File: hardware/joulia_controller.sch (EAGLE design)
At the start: 46 parts, among them IC1 LM2902D, IC2 LM2902D, U1 MMBT2222ALT1G, U2 MMBT2222ALT1G

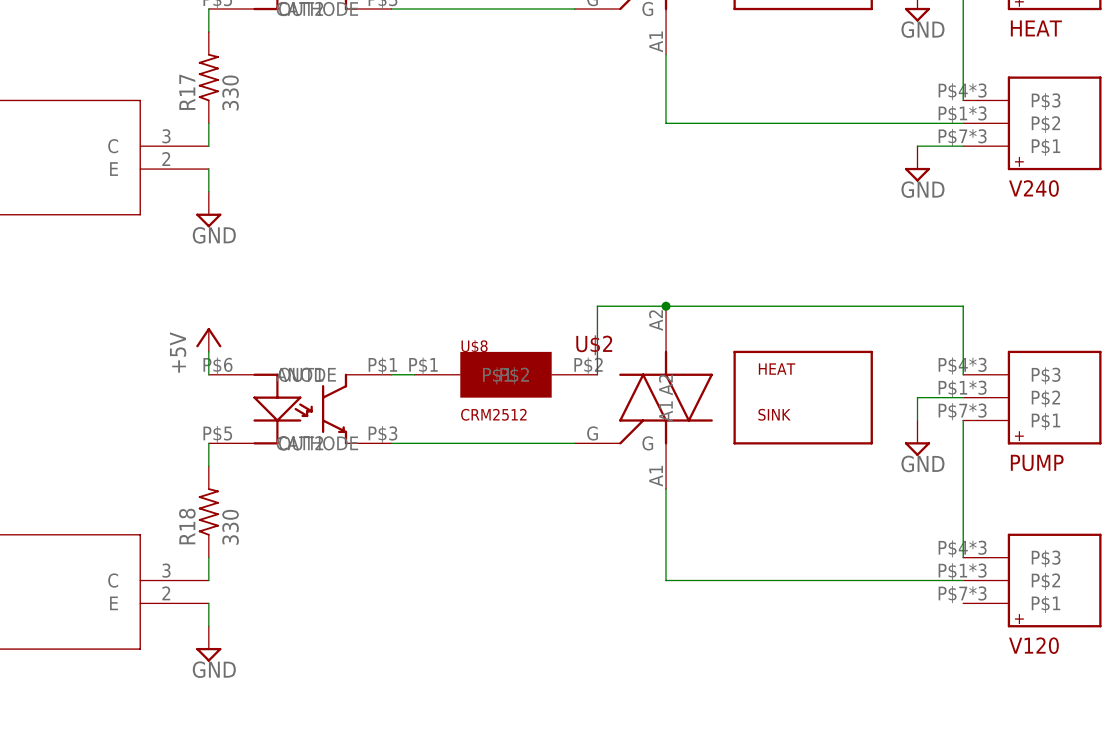
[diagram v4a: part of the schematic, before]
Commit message: Switching to mechanical relay for pump and horizontal heatsink.
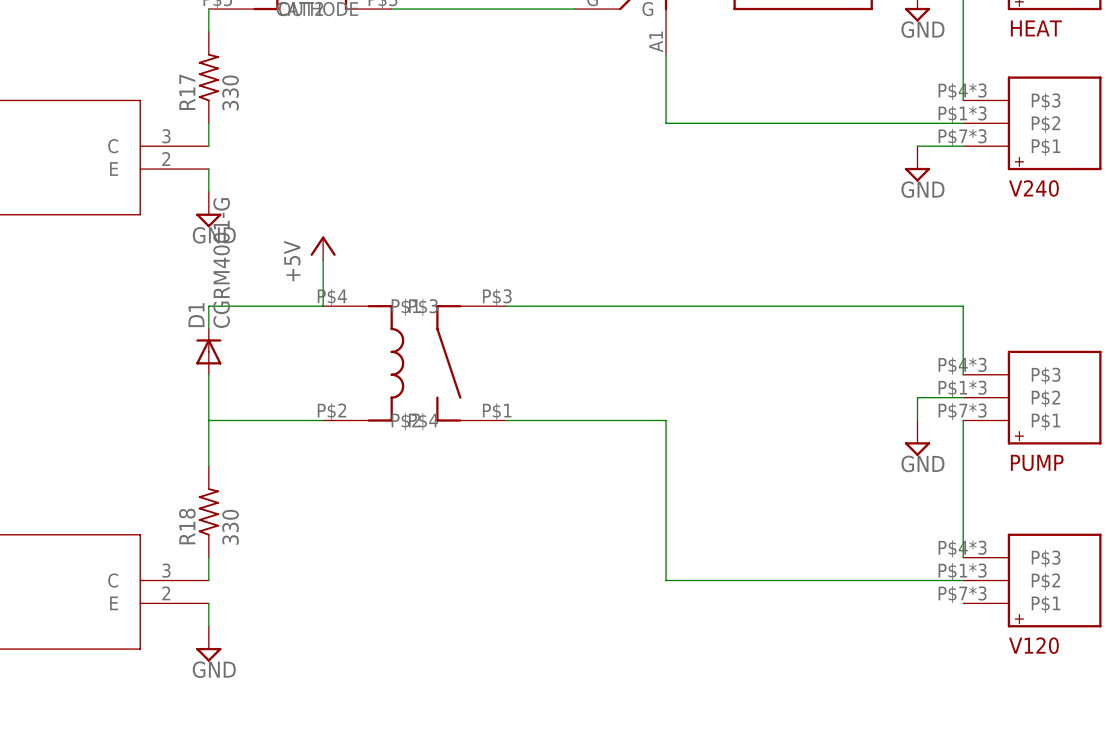
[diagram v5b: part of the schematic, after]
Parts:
- removed HE_HEATSINK, P_HEATSINK: VM1-038-1AE, digikey:VM1-038-1AE
- removed U$6: MOC3020S, digikey:MOC3020S
- removed U$8: CRM2512, digikey:CRM2512
- added D1: CGRM4001-G, diode:CGRM4001-G
- added U$3: G5LE-1A4_DC5, digikey:G5LE-1A4_DC5
- U$2: value T3050H-6I -> VM1-038-1AEHORIZONTAL; device digikey:T3050H-6I -> digikey:VM1-038-1AEHORIZONTAL
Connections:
- removed net N$21: U$6.OUT1, U$8.P$1
- removed net N$23: U$2.G, U$6.OUT2
- net +5V: now also D1.C, U$3.P$1; no longer U$6.ANODE
- net 120H: now also U$3.P$4; no longer U$2.A1
- net N$17: now also D1.A, U$3.P$2; no longer U$6.CATHODE
- net N$24: now also U$3.P$3; no longer U$2.A2, U$8.P$2
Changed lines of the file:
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@@
 <part name="R16" library="resistor" library_urn="urn:adsk.eagle:library:348" deviceset="R-US_" device="R0402" value="1K"/>
 <part name="U$1" library="digikey" deviceset="T3050H-6I" device=""/>
-<part name="U$2" library="digikey" deviceset="T3050H-6I" device=""/>
-<part name="HE_HEATSINK" library="digikey" deviceset="VM1-038-1AE" device=""/>
-<part name="P_HEATSINK" library="digikey" deviceset="VM1-038-1AE" device=""/>
 <part name="U$5" library="digikey" deviceset="MOC3020S" device=""/>
-<part name="U$6" library="digikey" deviceset="MOC3020S" device=""/>
 <part name="U$7" library="digikey" deviceset="CRM2512" device=""/>
-<part name="U$8" library="digikey" deviceset="CRM2512" device=""/>
 <part name="P+1" library="supply1" library_urn="urn:adsk.eagle:library:371" deviceset="+5V" device=""/>
 <part name="P+2" library="supply1" library_urn="urn:adsk.eagle:library:371" deviceset="+5V" device=""/>
@@
 <part name="SUPPLY22" library="supply2" deviceset="GND" device=""/>
 <part name="P+8" library="supply1" library_urn="urn:adsk.eagle:library:371" deviceset="+5V" device=""/>
+<part name="U$3" library="digikey" deviceset="G5LE-1A4_DC5" device=""/>
+<part name="U$2" library="digikey" deviceset="VM1-038-1AE" device="HORIZONTAL"/>
+<part name="D1" library="diode" library_urn="urn:adsk.eagle:library:210" deviceset="CGRM400*-G" device="" technology="1"/>
 </parts>
 <sheets>
@@
 <instance part="R16" gate="G$1" x="190.5" y="55.88" rot="R180"/>
 <instance part="U$1" gate="G$1" x="292.1" y="124.46"/>
-<instance part="U$2" gate="G$1" x="292.1" y="76.2"/>
-<instance part="HE_HEATSINK" gate="G$1" x="309.88" y="124.46"/>
-<instance part="P_HEATSINK" gate="G$1" x="309.88" y="76.2"/>
 <instance part="U$5" gate="G$1" x="256.54" y="121.92"/>
-<instance part="U$6" gate="G$1" x="256.54" y="73.66"/>
 <instance part="U$7" gate="G$1" x="276.86" y="127"/>
-<instance part="U$8" gate="G$1" x="276.86" y="78.74"/>
 <instance part="P+1" gate="1" x="243.84" y="132.08"/>
-<instance part="P+2" gate="1" x="243.84" y="83.82"/>
+<instance part="P+2" gate="1" x="256.54" y="93.98"/>
 <instance part="HEAT" gate="G$1" x="332.74" y="124.46" rot="MR180"/>
 <instance part="PUMP" gate="G$1" x="332.74" y="76.2" rot="MR180"/>
@@
 <instance part="SUPPLY22" gate="GND" x="121.92" y="35.56"/>
 <instance part="P+8" gate="1" x="139.7" y="43.18"/>
+<instance part="U$3" gate="G$1" x="264.16" y="81.28"/>
+<instance part="U$2" gate="G$1" x="309.88" y="124.46"/>
+<instance part="D1" gate="G$1" x="243.84" y="81.28" rot="R90"/>
 </instances>
 <busses>
@@
 </segment>
 <segment>
-<pinref part="U$6" gate="G$1" pin="ANODE"/>
 <pinref part="P+2" gate="1" pin="+5V"/>
-<wire x1="243.84" y1="78.74" x2="243.84" y2="81.28" width="0.1524" layer="91"/>
+<wire x1="256.54" y1="86.36" x2="256.54" y2="91.44" width="0.1524" layer="91"/>
+<pinref part="U$3" gate="G$1" pin="P$1"/>
+<pinref part="D1" gate="G$1" pin="C"/>
+<wire x1="243.84" y1="83.82" x2="243.84" y2="86.36" width="0.1524" layer="91"/>
+<wire x1="243.84" y1="86.36" x2="256.54" y2="86.36" width="0.1524" layer="91"/>
 </segment>
 <segment>
@@
 </segment>
 </net>
-<net name="N$21" class="1">
-<segment>
-<pinref part="U$6" gate="G$1" pin="OUT1"/>
-<pinref part="U$8" gate="G$1" pin="P$1"/>
-<wire x1="266.7" y1="78.74" x2="264.16" y2="78.74" width="0.1524" layer="91"/>
-</segment>
-</net>
 <net name="N$22" class="2">
 <segment>
@@
 </segment>
 </net>
-<net name="N$23" class="1">
-<segment>
-<pinref part="U$6" gate="G$1" pin="OUT2"/>
-<pinref part="U$2" gate="G$1" pin="G"/>
-<wire x1="264.16" y1="71.12" x2="284.48" y2="71.12" width="0.1524" layer="91"/>
-</segment>
-</net>
 <net name="N$24" class="1">
 <segment>
-<pinref part="U$8" gate="G$1" pin="P$2"/>
-<wire x1="287.02" y1="78.74" x2="287.02" y2="86.36" width="0.1524" layer="91"/>
-<pinref part="U$2" gate="G$1" pin="A2"/>
-<wire x1="287.02" y1="86.36" x2="294.64" y2="86.36" width="0.1524" layer="91"/>
 <pinref part="PUMP" gate="G$1" pin="P$3"/>
 <wire x1="327.66" y1="78.74" x2="327.66" y2="86.36" width="0.1524" layer="91"/>
-<wire x1="327.66" y1="86.36" x2="294.64" y2="86.36" width="0.1524" layer="91"/>
-<junction x="294.64" y="86.36"/>
+<wire x1="327.66" y1="86.36" x2="276.86" y2="86.36" width="0.1524" layer="91"/>
+<pinref part="U$3" gate="G$1" pin="P$3"/>
 </segment>
 </net>
 <net name="120H" class="1">
 <segment>
-<pinref part="U$2" gate="G$1" pin="A1"/>
 <pinref part="V120" gate="G$1" pin="P$2"/>
 <wire x1="327.66" y1="55.88" x2="294.64" y2="55.88" width="0.1524" layer="91"/>
-<wire x1="294.64" y1="55.88" x2="294.64" y2="66.04" width="0.1524" layer="91"/>
+<wire x1="294.64" y1="55.88" x2="294.64" y2="73.66" width="0.1524" layer="91"/>
+<pinref part="U$3" gate="G$1" pin="P$4"/>
+<wire x1="276.86" y1="73.66" x2="294.64" y2="73.66" width="0.1524" layer="91"/>
 </segment>
 </net>
@@
 <net name="N$17" class="0">
 <segment>
-<pinref part="U$6" gate="G$1" pin="CATHODE"/>
-<wire x1="243.84" y1="68.58" x2="243.84" y2="71.12" width="0.1524" layer="91"/>
+<wire x1="243.84" y1="68.58" x2="243.84" y2="73.66" width="0.1524" layer="91"/>
+<wire x1="243.84" y1="73.66" x2="256.54" y2="73.66" width="0.1524" layer="91"/>
 <pinref part="R18" gate="G$1" pin="2"/>
-</segment>
-</net>
+<pinref part="U$3" gate="G$1" pin="P$2"/>
+<pinref part="D1" gate="G$1" pin="A"/>
+<wire x1="243.84" y1="73.66" x2="243.84" y2="78.74" width="0.1524" layer="91"/>
+</segment>
+</net>

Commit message: Removing extraneous resistor for relay.
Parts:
- removed R18: 330, resistor:R-US_R1206
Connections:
- removed net N$17: D1.A, R18.2, U$3.P$2
- net N$18: now also D1.A, U$3.P$2; no longer R18.1
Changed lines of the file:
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@@
 <part name="SUPPLY19" library="supply2" library_urn="urn:adsk.eagle:library:372" deviceset="GND" device=""/>
 <part name="R17" library="resistor" library_urn="urn:adsk.eagle:library:348" deviceset="R-US_" device="R1206" value="330"/>
-<part name="R18" library="resistor" library_urn="urn:adsk.eagle:library:348" deviceset="R-US_" device="R1206" value="330"/>
 <part name="HELED" library="eagle-ltspice" library_urn="urn:adsk.eagle:library:217" deviceset="LED_E" device="SML0603"/>
 <part name="PPLED" library="eagle-ltspice" library_urn="urn:adsk.eagle:library:217" deviceset="LED_E" device="SML0603"/>
@@
 <instance part="SUPPLY19" gate="GND" x="322.58" y="101.6"/>
 <instance part="R17" gate="G$1" x="243.84" y="111.76" rot="R90"/>
-<instance part="R18" gate="G$1" x="243.84" y="63.5" rot="R90"/>
 <instance part="HELED" gate="G$1" x="185.42" y="88.9"/>
 <instance part="PPLED" gate="G$1" x="185.42" y="40.64"/>
@@
 </segment>
 </net>
-<net name="N$17" class="0">
-<segment>
-<wire x1="243.84" y1="68.58" x2="243.84" y2="73.66" width="0.1524" layer="91"/>
+<net name="N$18" class="0">
+<segment>
+<pinref part="U2" gate="A" pin="C"/>
 <wire x1="243.84" y1="73.66" x2="256.54" y2="73.66" width="0.1524" layer="91"/>
-<pinref part="R18" gate="G$1" pin="2"/>
 <pinref part="U$3" gate="G$1" pin="P$2"/>
 <pinref part="D1" gate="G$1" pin="A"/>
 <wire x1="243.84" y1="73.66" x2="243.84" y2="78.74" width="0.1524" layer="91"/>
-</segment>
-</net>
-<net name="N$18" class="0">
-<segment>
-<pinref part="U2" gate="A" pin="C"/>
-<wire x1="243.84" y1="55.88" x2="243.84" y2="58.42" width="0.1524" layer="91"/>
-<pinref part="R18" gate="G$1" pin="1"/>
-</segment>
-</net>
+<wire x1="243.84" y1="55.88" x2="243.84" y2="73.66" width="0.1524" layer="91"/>
+</segment>
+</net>

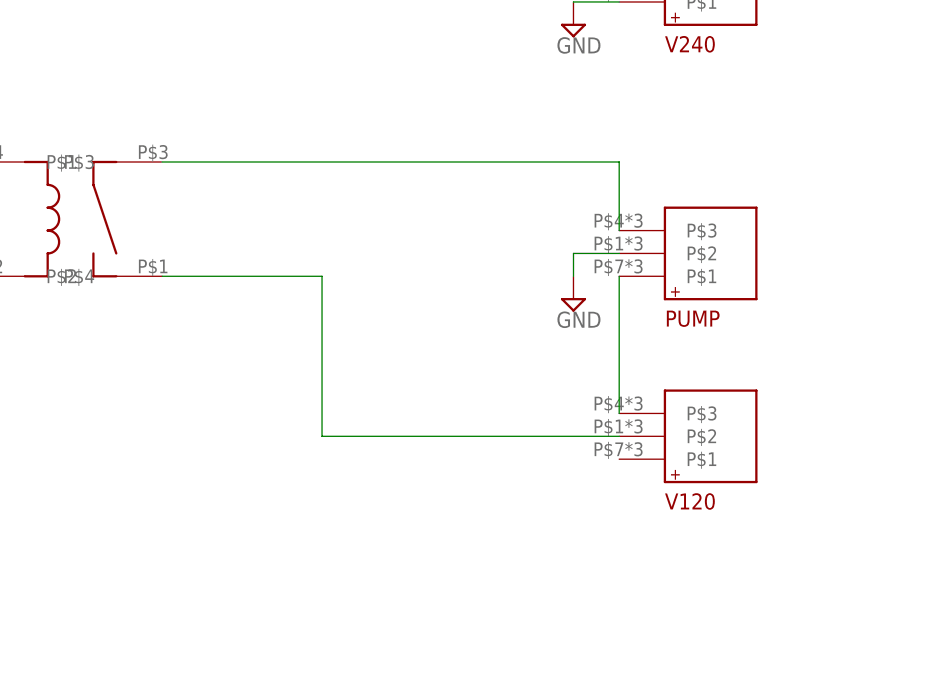
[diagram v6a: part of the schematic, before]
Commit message: Switches two plugs for one board terminal for 120V connections.
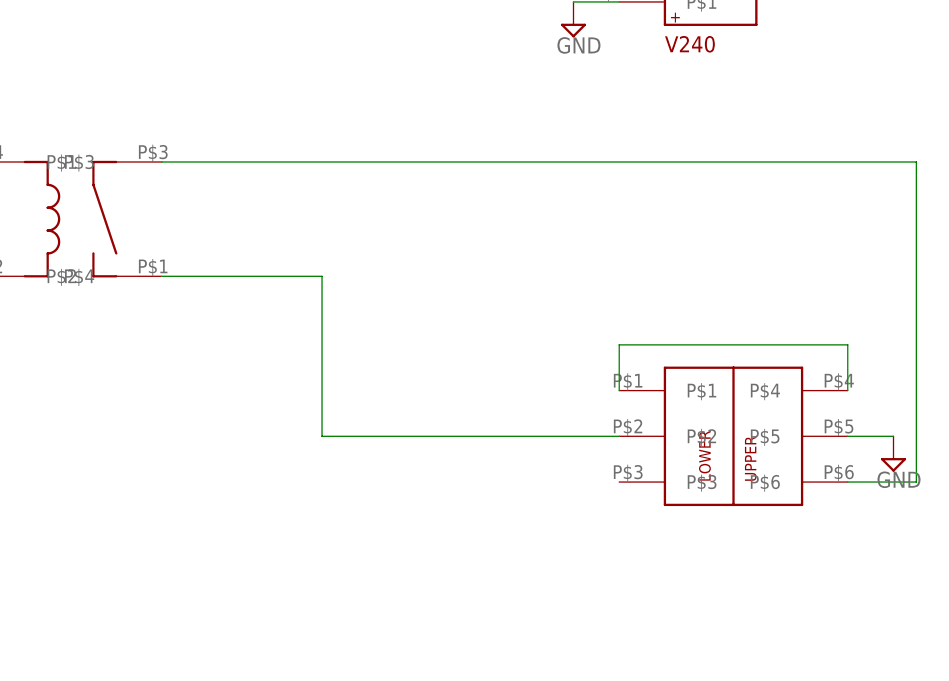
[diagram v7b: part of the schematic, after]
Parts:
- removed PUMP, V120: PC1720589, digikey:PC1720589
- added U$4: PC1725041, digikey:PC1725041
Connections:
- net 120H: now also U$4.P$2; no longer V120.P$2
- net 120N: now also U$4.P$1, U$4.P$4; no longer PUMP.P$1, V120.P$3
- net GND: now also U$4.P$5; no longer PUMP.P$2
- net N$24: now also U$4.P$6; no longer PUMP.P$3
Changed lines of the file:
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@@
 <part name="P+2" library="supply1" library_urn="urn:adsk.eagle:library:371" deviceset="+5V" device=""/>
 <part name="HEAT" library="digikey" deviceset="PC1720589" device=""/>
-<part name="PUMP" library="digikey" deviceset="PC1720589" device=""/>
 <part name="SUPPLY17" library="supply2" library_urn="urn:adsk.eagle:library:372" deviceset="GND" device=""/>
 <part name="SUPPLY18" library="supply2" library_urn="urn:adsk.eagle:library:372" deviceset="GND" device=""/>
 <part name="V240" library="digikey" deviceset="PC1720589" device=""/>
-<part name="V120" library="digikey" deviceset="PC1720589" device=""/>
 <part name="SUPPLY19" library="supply2" library_urn="urn:adsk.eagle:library:372" deviceset="GND" device=""/>
 <part name="R17" library="resistor" library_urn="urn:adsk.eagle:library:348" deviceset="R-US_" device="R1206" value="330"/>
@@
 <part name="U$2" library="digikey" deviceset="VM1-038-1AE" device="HORIZONTAL"/>
 <part name="D1" library="diode" library_urn="urn:adsk.eagle:library:210" deviceset="CGRM400*-G" device="" technology="1"/>
+<part name="U$4" library="digikey" deviceset="PC1725041" device=""/>
 </parts>
 <sheets>
@@
 <instance part="P+2" gate="1" x="256.54" y="93.98"/>
 <instance part="HEAT" gate="G$1" x="332.74" y="124.46" rot="MR180"/>
-<instance part="PUMP" gate="G$1" x="332.74" y="76.2" rot="MR180"/>
 <instance part="SUPPLY17" gate="GND" x="322.58" y="119.38"/>
-<instance part="SUPPLY18" gate="GND" x="322.58" y="71.12"/>
+<instance part="SUPPLY18" gate="GND" x="358.14" y="53.34"/>
 <instance part="V240" gate="G$1" x="332.74" y="106.68" rot="MR180"/>
-<instance part="V120" gate="G$1" x="332.74" y="55.88" rot="MR180"/>
 <instance part="SUPPLY19" gate="GND" x="322.58" y="101.6"/>
 <instance part="R17" gate="G$1" x="243.84" y="111.76" rot="R90"/>
@@
 <instance part="U$2" gate="G$1" x="309.88" y="124.46"/>
 <instance part="D1" gate="G$1" x="243.84" y="81.28" rot="R90"/>
+<instance part="U$4" gate="G$1" x="340.36" y="55.88"/>
 </instances>
 <busses>
@@
 </segment>
 <segment>
-<pinref part="PUMP" gate="G$1" pin="P$2"/>
-<wire x1="327.66" y1="76.2" x2="322.58" y2="76.2" width="0.1524" layer="91"/>
-<wire x1="322.58" y1="76.2" x2="322.58" y2="73.66" width="0.1524" layer="91"/>
+<wire x1="353.06" y1="55.88" x2="358.14" y2="55.88" width="0.1524" layer="91"/>
 <pinref part="SUPPLY18" gate="GND" pin="GND"/>
+<pinref part="U$4" gate="G$1" pin="P$5"/>
 </segment>
 <segment>
@@
 <net name="N$24" class="1">
 <segment>
-<pinref part="PUMP" gate="G$1" pin="P$3"/>
-<wire x1="327.66" y1="78.74" x2="327.66" y2="86.36" width="0.1524" layer="91"/>
-<wire x1="327.66" y1="86.36" x2="276.86" y2="86.36" width="0.1524" layer="91"/>
+<wire x1="360.68" y1="86.36" x2="276.86" y2="86.36" width="0.1524" layer="91"/>
 <pinref part="U$3" gate="G$1" pin="P$3"/>
+<wire x1="360.68" y1="86.36" x2="360.68" y2="50.8" width="0.1524" layer="91"/>
+<pinref part="U$4" gate="G$1" pin="P$6"/>
+<wire x1="360.68" y1="50.8" x2="353.06" y2="50.8" width="0.1524" layer="91"/>
 </segment>
 </net>
 <net name="120H" class="1">
 <segment>
-<pinref part="V120" gate="G$1" pin="P$2"/>
 <wire x1="327.66" y1="55.88" x2="294.64" y2="55.88" width="0.1524" layer="91"/>
 <wire x1="294.64" y1="55.88" x2="294.64" y2="73.66" width="0.1524" layer="91"/>
 <pinref part="U$3" gate="G$1" pin="P$4"/>
 <wire x1="276.86" y1="73.66" x2="294.64" y2="73.66" width="0.1524" layer="91"/>
+<pinref part="U$4" gate="G$1" pin="P$2"/>
 </segment>
 </net>
@@
 <net name="120N" class="1">
 <segment>
-<pinref part="PUMP" gate="G$1" pin="P$1"/>
-<pinref part="V120" gate="G$1" pin="P$3"/>
-<wire x1="327.66" y1="73.66" x2="327.66" y2="58.42" width="0.1524" layer="91"/>
-</segment>
-</net>
+<wire x1="327.66" y1="66.04" x2="327.66" y2="60.96" width="0.1524" layer="91"/>
+<pinref part="U$4" gate="G$1" pin="P$1"/>
+<wire x1="327.66" y1="66.04" x2="353.06" y2="66.04" width="0.1524" layer="91"/>
+<wire x1="353.06" y1="66.04" x2="353.06" y2="60.96" width="0.1524" layer="91"/>
+<pinref part="U$4" gate="G$1" pin="P$4"/>
+</segment>
+</net>
